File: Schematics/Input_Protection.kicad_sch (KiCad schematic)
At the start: 11 parts, among them J21 43650-0418, J22 464369202, Q6 STB10NK60ZT4

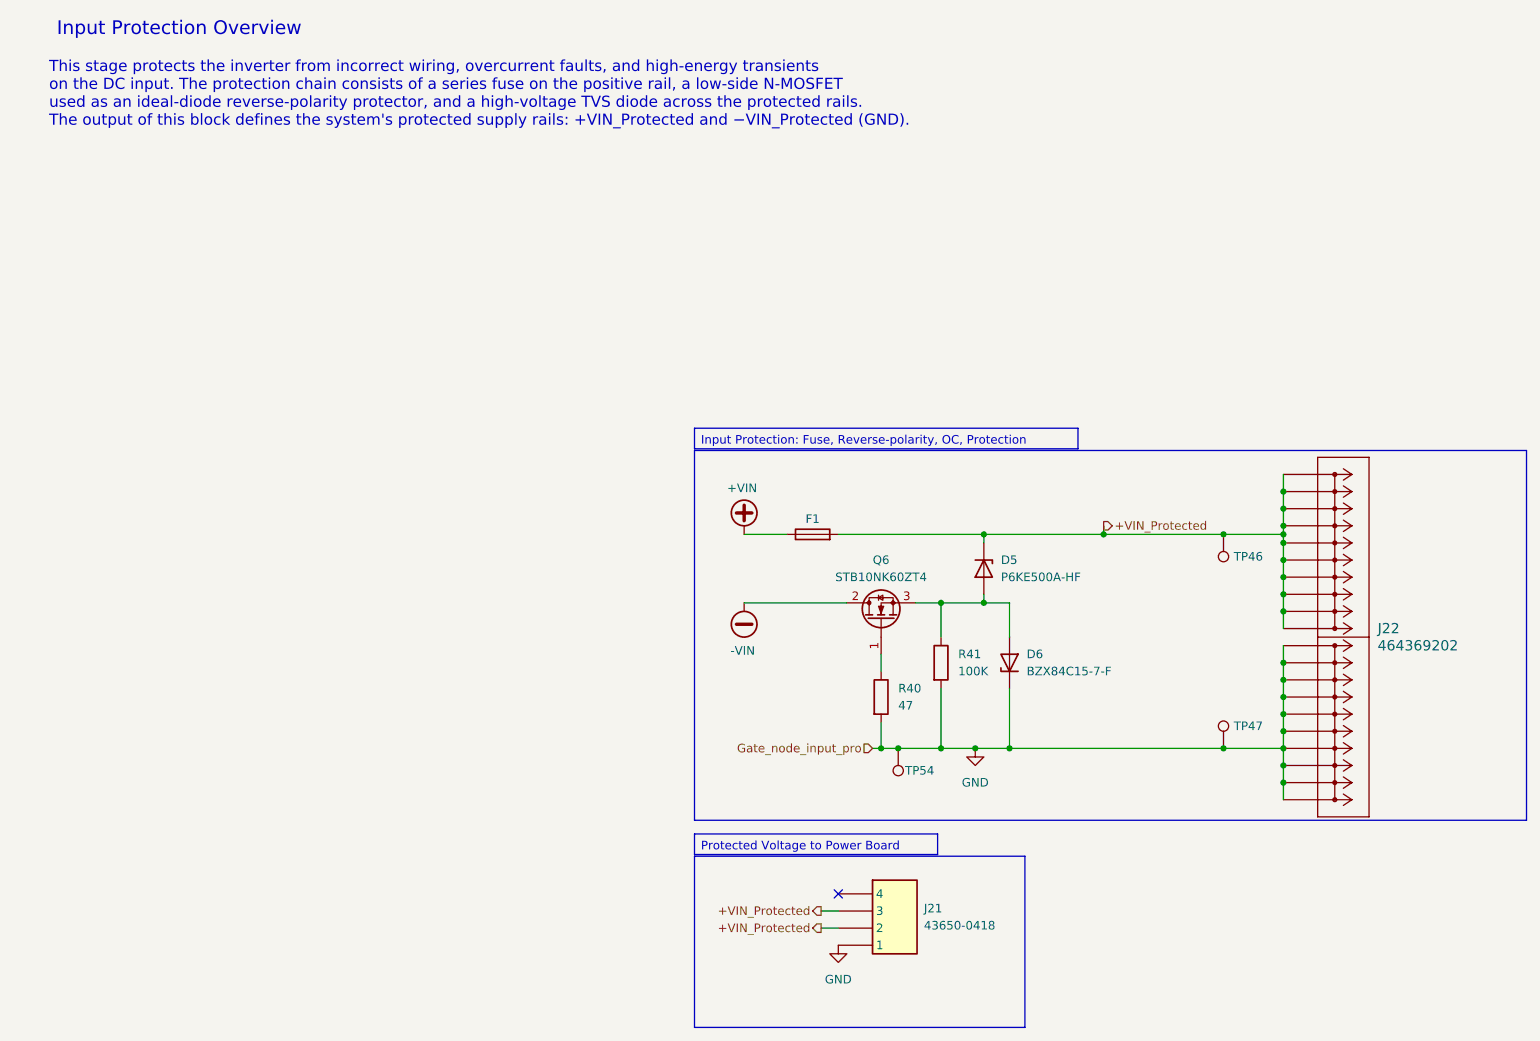
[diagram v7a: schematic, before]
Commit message: [WIP Input Protection Circuit to Controller]
- Added Gate node input protection pin to controller
- Added optocoupler to input protection circuit
- Added 3d model for PC817.....
- Updated PCB to test out PCB modularity
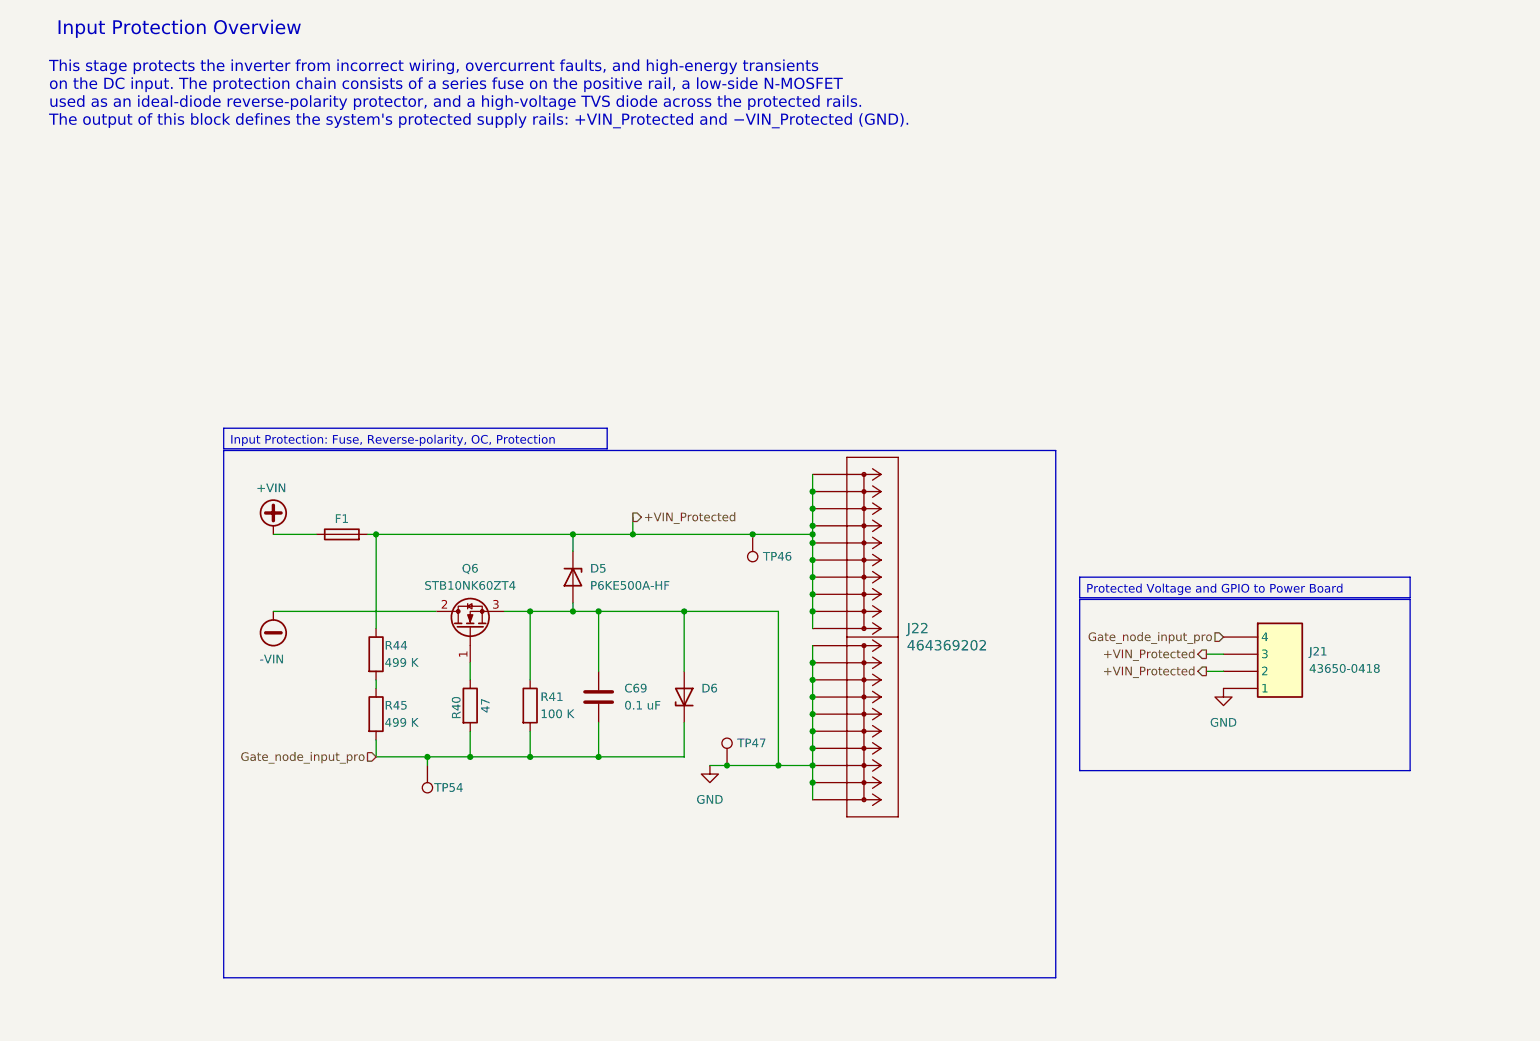
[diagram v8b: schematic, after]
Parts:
- added C69: 0.1 uF, Capacitor_SMD:C_0805_2012Metric_Pad1.18x1.45mm_HandSolder, symbol SiC_Inverter:C2012X8R1E105M125AE
- added R44, R45: 499 K, Resistor_SMD:R_1206_3216Metric_Pad1.30x1.75mm_HandSolder, symbol SiC_Inverter:RP1206BRD07499KL
- R40: symbol Device:R -> SiC_Inverter:RT1206FRE0747RL
- R41: value 100K -> 100 K; symbol Device:R -> SiC_Inverter:RT1206BRD07100KL
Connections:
- net +VIN_Protected: now also R44.1
- net GND: now also D5.2 (A), D6.2 (A), Q6.3, R41.1, C69.1; no longer D6.1 (K), R40.2, R41.2, TP54.1
- net Gate_node_input_pro: now reaches J21.4
- net Gate_node_input_pro: now also D6.1 (K), R40.2, R41.2, TP54.1, C69.2, R45.2
- new net: R44.2, R45.1
- no-connect marks 1 -> 0
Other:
- moved on the sheet: D5, D6, F1, J21, J22, Q6, R40, R41, TP46, TP47, TP54
